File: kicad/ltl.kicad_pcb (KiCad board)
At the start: 2 copper layers, 95 x 70 mm, 56 parts, among them J1 Conn_01x06, J2 Conn_01x15, J3 Conn_01x04, Q1 RUM001L02T2CL, Q2 RZM001P02T2L, Q3 BC327, U1 TPL5111, U2 ESP-12E, U3 DS18B20, U4 TPS73733DCQR

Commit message: Updated Readme
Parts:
- removed kibuzzard-65AD85A3: G***, kibuzzard-65AD85A3
- added D2: LED Green, LED_THT:LED_D3.0mm_Clear, F.Cu at (126.6, 84.5)
- added D3: LED Red, LED_THT:LED_D3.0mm_Clear, F.Cu at (77.4, 81.5)
- added J1: Charger, Connector_PinHeader_2.54mm:PinHeader_1x03_P2.54mm_Vertical, F.Cu at (130.4, 133.0)
- added R17: 2k, Resistor_THT:R_Axial_DIN0207_L6.3mm_D2.5mm_P10.16mm_Horizontal, F.Cu at (118.2, 79.2)
- added R20: 2k, Resistor_THT:R_Axial_DIN0207_L6.3mm_D2.5mm_P10.16mm_Horizontal, F.Cu at (103.9, 69.8)
- added TP1: Done, TestPoint:TestPoint_Loop_D1.80mm_Drill1.0mm_Beaded, F.Cu at (100.3, 83.5)
- added TP2: Drive, TestPoint:TestPoint_Loop_D1.80mm_Drill1.0mm_Beaded, F.Cu at (100.3, 89.4)
- added TP3: BatDiv, TestPoint:TestPoint_Loop_D1.80mm_Drill1.0mm_Beaded, F.Cu at (118.2, 84.8)
- added TP4: Flash, TestPoint:TestPoint_Loop_D1.80mm_Drill1.0mm_Beaded, F.Cu at (129.8, 74.2)
- added TP5: Reset, TestPoint:TestPoint_Loop_D1.80mm_Drill1.0mm_Beaded, F.Cu at (157.9, 74.2)
- BT1: value 18650 -> 1042; footprint 18650:18650_small -> keystone_18650:BAT_1042
- C8: renamed from C1; value 10uF -> 100uF
- H1, H2, H3, H4, H5, H6: value MountingHole -> MountingHole_Pad
- Q1: renamed from Q3; footprint Package_TO_SOT_THT:TO-92_Inline -> Package_TO_SOT_THT:TO-92_Inline_Wide
- R18: renamed from R14; value 49.9k -> 39K
- U1: value TPL5111 -> TPL5111DDCR
- moved J4 12.0 mm to (99.2, 70.2), turned to -90 degrees
- moved Q1 4.59 mm to (122.4, 105.0)
- moved U4 3.11 mm to (167.9, 85.4), turned to 180 degrees
- moved Reset1 1.61 mm to (154.1, 76.4)
- moved C10 0.82 mm to (146.0, 86.2)
- moved R8 0.32 mm to (133.2, 86.4)
- moved R9 0.32 mm to (133.2, 89.5)
- moved BT1 0.23 mm to (125.8, 118.5), turned to 180 degrees
- moved R10 0.23 mm to (133.2, 92.8)
- moved R16 0.18 mm to (133.2, 95.9)
- moved R11 0.17 mm to (133.2, 99.0)
- moved R14 0.12 mm to (133.2, 102.2)
- moved Flash1 0.11 mm to (139.9, 76.4)
- moved R15 0.05 mm to (133.2, 105.4)
- renumbered C10 to C1, C9 to C10, C7 to C11, C8 to C12, C11 to C2, C12 to C3, C2 to C4, C3 to C5, C4 to C6, C5 to C7, C6 to C9, J3 to J2, J2 to J3, J1 to J4, Q1 to Q2, Q2 to Q3, R8 to R1, R3 to R10, R5 to R11, R6 to R14, R7 to R15, R4 to R16, R15 to R19, R16 to R2, R17 to R3, R11 to R4, R9 to R5, R10 to R6, R18 to R7, R1 to R8, R2 to R9, U4 to U2, U2 to U3, U3 to U4
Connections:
- C1 pad 2: GND -> RESET
- H1 pad 1: (no net) -> GND
- H2 pad 1: (no net) -> GND
- H3 pad 1: (no net) -> GND
- H4 pad 1: (no net) -> GND
- H5 pad 1: (no net) -> GND
- H6 pad 1: (no net) -> GND
- J3 pad 13: GPIO12 -> GPIO2
- J4 pad 1: unconnected-(J1-Pin_1-Pad1) -> GND
- J4 pad 2: GND -> unconnected-(J4-Pin_2-Pad2)
- R16 pad 2: Net-(U2-GPIO2) -> GPIO12
- U3 pad 11: Net-(U2-GPIO2) -> GPIO2
- U4 pad 2: Net-(U2-GPIO2) -> GPIO12
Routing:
- net GND: track 343.9 -> 487.0 mm, vias 0 -> 1
- net GPIO14: track 0.00 -> 112.2 mm
- net GPIO16: track 0.00 -> 95.4 mm, vias 0 -> 1
- net GPIO2: track 0.00 -> 81.9 mm
- net +4V: track 114.5 -> 191.7 mm, vias 2 -> 1
- net Net-(J3-Pin_8): track 0.00 -> 75.2 mm
- net GPIO12: track 94.3 -> 29.4 mm
- net Net-(J1-Pin_2): track 0.00 -> 54.9 mm
- net Net-(U2-GPIO2): track 45.3 -> 0.00 mm, vias 1 -> 0
- net Net-(D3-A): track 0.00 -> 43.6 mm
- net +3V3: track 221.0 -> 178.2 mm, vias 0 -> 3
- net RESET: track 35.8 -> 64.8 mm
- net SDA: track 117.3 -> 141.6 mm, vias 1 -> 0
- net Net-(U3-RXD): track 0.00 -> 18.7 mm
- net FLASH: track 45.9 -> 62.9 mm, vias 0 -> 1
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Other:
- outline, holes or cut-outs redrawn
- board text added: "10"
- board text added: "13"
- board text added: "14"
- board text added: "2"
- board text added: "Flash Circuit"
- board text added: "Rev. 2.3"
- board text removed: "GPIO10"
- board text removed: "GPIO12"
- board text removed: "GPIO13"
- board text removed: "GPIO14"
- board text removed: "Rev. 2.2"

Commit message: A couple of addictions
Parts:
- removed D2: LED Green, LED_THT:LED_D3.0mm_Clear
- removed D3: LED Red, LED_THT:LED_D3.0mm_Clear
- removed the R17 at (118.2, 79.2)
- removed R20: 2k, Resistor_THT:R_Axial_DIN0207_L6.3mm_D2.5mm_P10.16mm_Horizontal
- added F1: Fuse_Small, Fuse:Fuse_1206_3216Metric_Pad1.42x1.75mm_HandSolder, F.Cu at (130.1, 133.0)
- J1: value Charger -> Conn_01x04; footprint Connector_PinHeader_2.54mm:PinHeader_1x03_P2.54mm_Vertical -> Connector_PinHeader_2.54mm:PinHeader_1x04_P2.54mm_Vertical
- J3: value Conn_01x15 -> Conn_01x16; footprint Connector_PinHeader_2.54mm:PinHeader_1x15_P2.54mm_Vertical -> Connector_PinHeader_2.54mm:PinHeader_1x16_P2.54mm_Vertical
- R1: value 42k -> 43K
- R10, R11, R12, R13, R4, R5, R6, R7, R8, R9: value 10k -> 10K
- R14, R15: value 1k -> 1K
- R16: value 4,7k -> 4.7K
- R18: renamed from R19; value 10k -> 10K
- moved J1 13.6 mm to (143.9, 133.0), turned to -90 degrees
- moved J3 2.56 mm to (77.1, 87.1)
- moved TP4 0.45 mm to (129.3, 74.2)
- renumbered R18 to R17
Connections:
- BT1 pad N: GND -> Net-(J1-Pin_2)
- BT1 pad P: Net-(J1-Pin_2) -> Net-(BT1-PadP)
- J1 pad 3: +4V -> unconnected-(J1-Pin_3-Pad3)
- J3 pad 10: GPIO16 -> Net-(J3-Pin_10)
- J3 pad 11: GPIO14 -> GPIO16
- J3 pad 12: GPIO13 -> GPIO14
- J3 pad 13: GPIO2 -> GPIO13
- J3 pad 2: +3V3 -> unconnected-(J3-Pin_2-Pad2)
- J3 pad 3: +4V -> +3V3
- J3 pad 4: SCL -> +4V
- J3 pad 5: SDA -> SCL
- J3 pad 6: Net-(J3-Pin_6) -> SDA
- U3 pad 17: Net-(J3-Pin_6) -> Net-(J3-Pin_7)
- U3 pad 18: Net-(J3-Pin_8) -> Net-(J3-Pin_9)
- U3 pad 21: Net-(J3-Pin_9) -> Net-(J3-Pin_10)
- U3 pad 22: Net-(J3-Pin_7) -> Net-(J3-Pin_8)
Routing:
- net Net-(J3-Pin_6): track 77.2 -> 0.00 mm
- net Net-(J3-Pin_10): track 0.00 -> 72.7 mm
- net Net-(BT1-PadP): track 0.00 -> 50.7 mm
- net Net-(D3-A): track 43.6 -> 0.00 mm
- net Net-(J3-Pin_14): track 83.1 -> 113.5 mm, vias 1 -> 0
- net Net-(J3-Pin_8): track 75.2 -> 99.5 mm, vias 0 -> 1
- net GPIO14: track 112.2 -> 88.0 mm, vias 0 -> 2
- net Net-(J1-Pin_2): track 54.9 -> 31.3 mm
- net GND: track 487.0 -> 504.6 mm, vias 1 -> 0
- net /TxD: track 59.4 -> 76.5 mm
- net /RxD: track 62.3 -> 77.3 mm
- net +4V: track 191.7 -> 179.2 mm, vias 1 -> 0
- net SCL: track 136.4 -> 124.9 mm
- net DTR: track 51.1 -> 61.8 mm
- net Net-(Q1-B): track 32.4 -> 22.7 mm
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- removed copper zone on B.Cu, net GND
- removed copper zone on F.Cu, net GND
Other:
- board text added: "BAT-"
- board text added: "GPIO2"
- board text added: "Rev: 2.4"
- board text added: "X"
- board text removed: "2"
- board text removed: "Rev. 2.3"

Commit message: Updated last image
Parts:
- BT1: footprint keystone_18650:BAT_1042 -> 18650:18650_flat
- moved BT1 0.39 mm to (125.5, 118.3)
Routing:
- net DONE: track 76.7 -> 133.5 mm, vias 2 -> 0
- net FLASH: track 63.9 -> 109.2 mm
- net Net-(J3-Pin_8): track 99.5 -> 73.8 mm, vias 1 -> 2
- net Net-(J3-Pin_14): track 113.5 -> 90.9 mm
- net GND: track 504.6 -> 486.3 mm
- net +4V: track 179.2 -> 163.2 mm, vias 0 -> 1
- net SDA: track 135.7 -> 122.4 mm, vias 0 -> 1
- net Net-(U1-~{DRV}): track 12.8 -> 24.0 mm
- net Net-(Q2-D): track 17.9 -> 26.8 mm, vias 1 -> 0
- net RESET: track 72.7 -> 64.8 mm
- net Net-(J3-Pin_10): track 72.7 -> 80.2 mm
- net SCL: track 124.9 -> 120.0 mm, vias 1 -> 0
- net DTR: track 61.8 -> 66.2 mm
- net +3V3: track 176.3 -> 180.0 mm
- net GPIO2: track 90.2 -> 87.2 mm
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
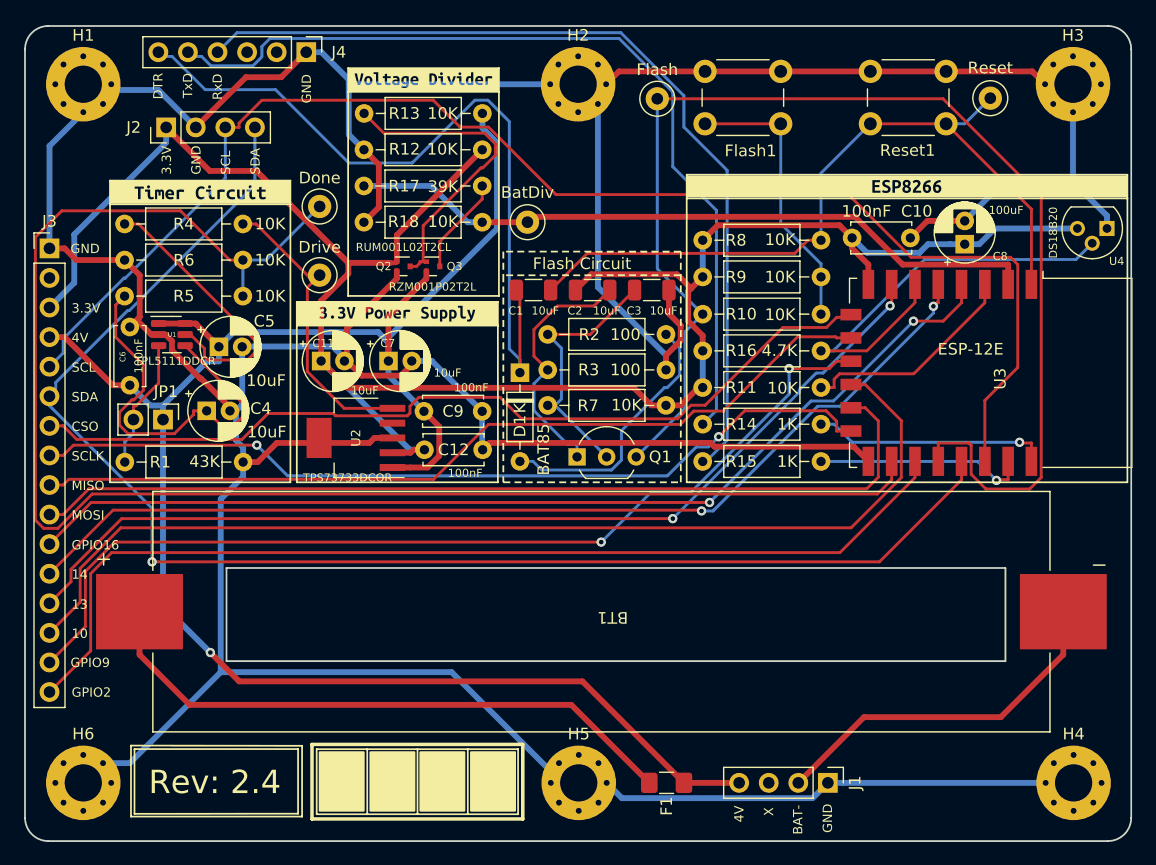
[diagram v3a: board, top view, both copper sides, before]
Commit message: Updated code to account for WiFi and MQTT broker outages and several other cleanups
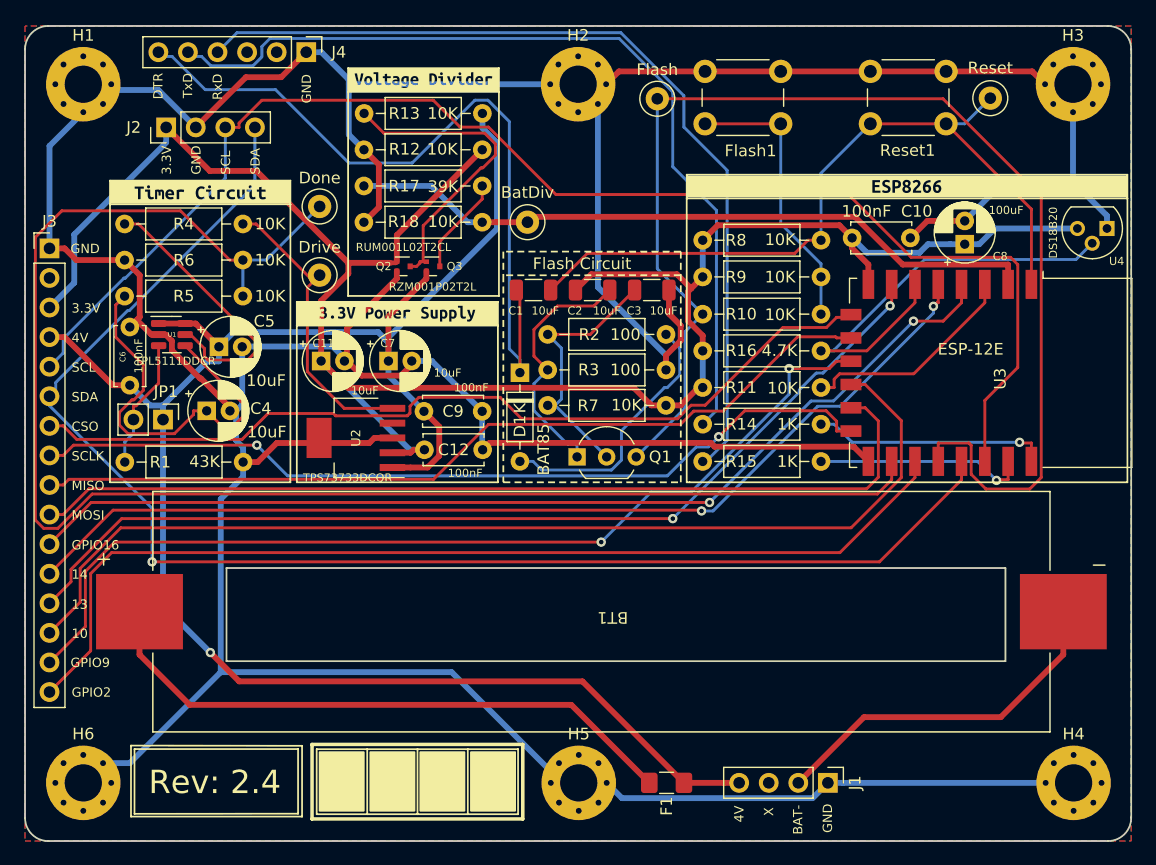
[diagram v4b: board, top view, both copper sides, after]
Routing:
- added copper zone on B.Cu, net GND
- added copper zone on F.Cu, net GND
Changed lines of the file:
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@@
     (fp_line (start 1.6 0.8) (end -1.6 0.8)
       (stroke (width 0.1) (type solid)) (layer "F.Fab"))
-    (pad "1" smd roundrect (at -1.4875 0) (size 1.425 1.75) (layers "F.Cu" "F.Paste" "F.Mask") (roundrect_rratio 0.175439)
+    (pad "1" smd roundrect (at -1.4875 0) (size 1.425 1.75) (layers "F.Cu" "F.Paste" "F.Mask") (roundrect_rratio 0.1754392982)
       (net 42 "Net-(BT1-PadP)") (pintype "passive"))
-    (pad "2" smd roundrect (at 1.4875 0) (size 1.425 1.75) (layers "F.Cu" "F.Paste" "F.Mask") (roundrect_rratio 0.175439)
+    (pad "2" smd roundrect (at 1.4875 0) (size 1.425 1.75) (layers "F.Cu" "F.Paste" "F.Mask") (roundrect_rratio 0.1754392982)
       (net 3 "+4V") (pintype "passive"))
     (model "${KICAD6_3DMODEL_DIR}/Fuse.3dshapes/Fuse_1206_3216Metric.wrl"
@@
   (segment (start 84.83 118.3) (end 84.83 121.9869) (width 0.5) (layer "F.Cu") (net 42))
   (segment (start 89.1449 126.3018) (end 84.83 121.9869) (width 0.5) (layer "F.Cu") (net 42))
+  (zone (net 1) (net_name "GND") (layers "F&B.Cu") (hatch edge 0.5)
+    (connect_pads (clearance 0))
+    (min_thickness 0.25) (filled_areas_thickness no)
+    (fill yes (thermal_gap 0.5) (thermal_bridge_width 0.5))
+    (polygon
+      (pts
+        (xy 170 68)
+        (xy 75 68)
+        (xy 75 138)
+        (xy 170 138)
+      )
+    )
+  )
 )
